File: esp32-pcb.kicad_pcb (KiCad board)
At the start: 2 copper layers, 25.2 x 59.4 mm, 50 parts, among them J1 Conn_01x15_Male, J2 Conn_01x15_Male, Q1 SI2333DDS-T1-GE3, Q2 BSS138Q-7-F, Q3 MMBT3904, Q4 MMBT3904, Q5 BSS138Q-7-F, SW1 RESET, SW2 USER, SW3 SW_DIP_x04, U1 XC6220B331MR, U2 ESP32-WROOM-32, U3 CP2102N-A01-GQFN24

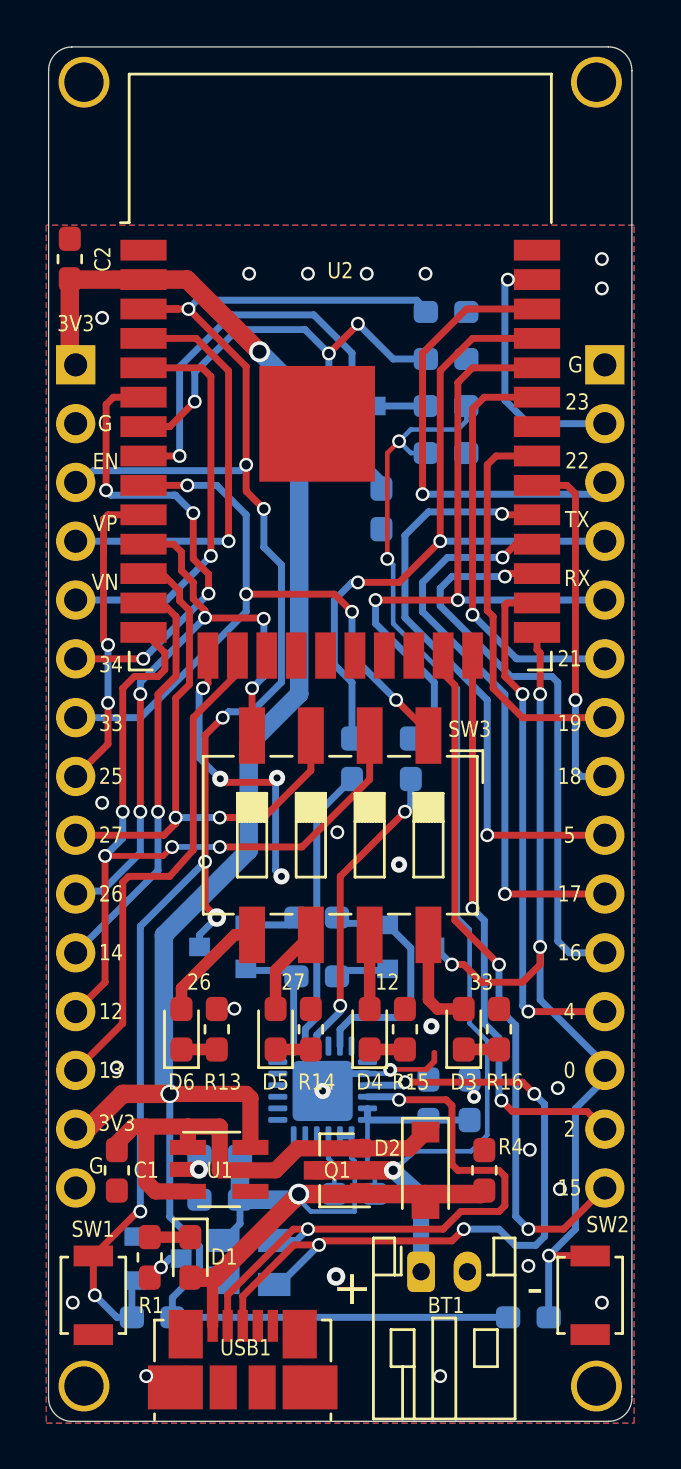
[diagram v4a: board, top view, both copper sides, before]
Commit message: Move C1 a bit, so that the left corner GND and 3V labels are more visible
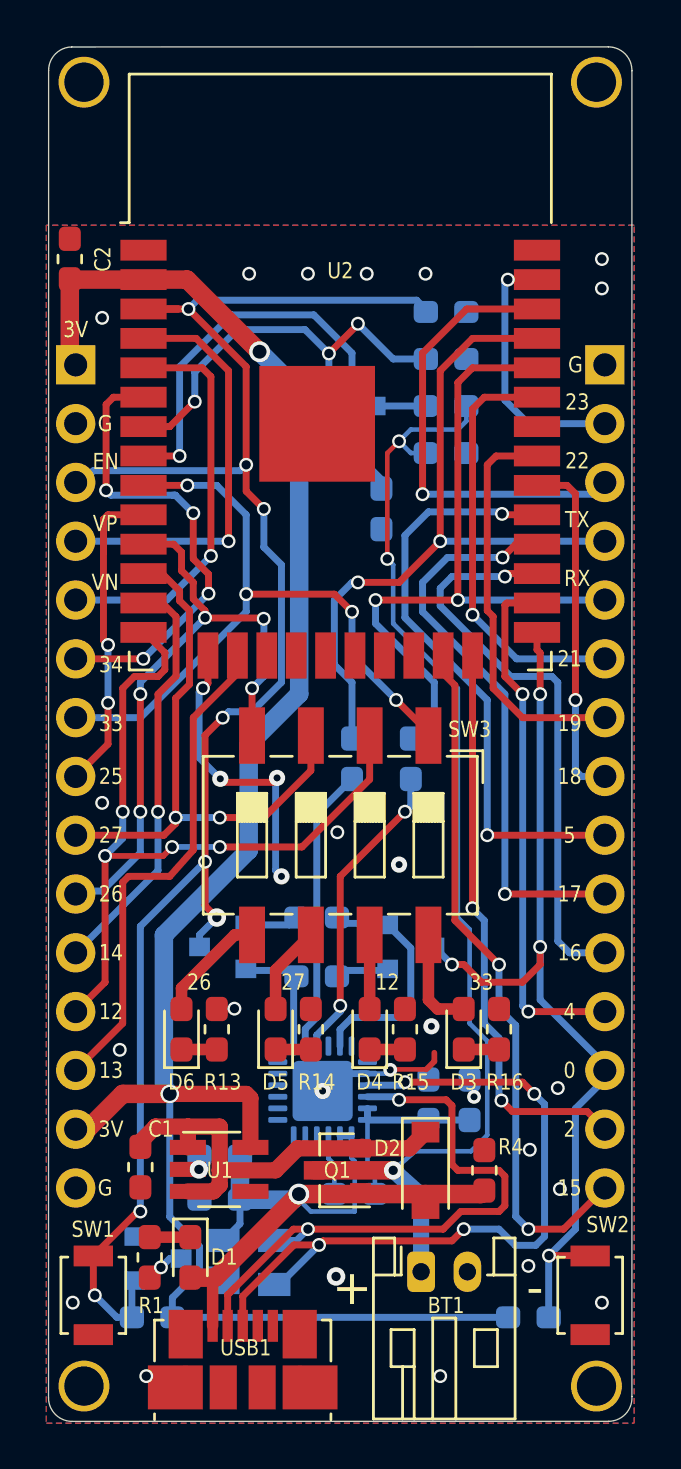
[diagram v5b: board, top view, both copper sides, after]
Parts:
- moved C1 1.03 mm to (133.1, 116.7)
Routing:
- net Net-(C1-Pad1): track 21.9 -> 18.5 mm
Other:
- board text added: "3V"
- board text removed: "3V3"
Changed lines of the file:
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@@
     (thickness 1.6)
     (drawings 3062)
-    (tracks 623)
+    (tracks 624)
     (zones 0)
     (modules 50)
@@
   )
   (setup
-    (last_trace_width 0.25)
+    (last_trace_width 0.7)
     (user_trace_width 0.2)
     (user_trace_width 0.25)
@@
   )
   (module Capacitor_SMD:C_0603_1608Metric_Pad1.05x0.95mm_HandSolder (layer F.Cu)
-    (at 132.08 116.84 270)
+    (at 133.096 116.699 270)
     (descr "Capacitor SMD 0603 (1608 Metric), square (rectangular) end terminal, IPC_7351 nominal with elongated pad for handsoldering. (Body size source: http://www.tortai-tech.com/upload/download/2011102023233369053.pdf), generated with kicad-footprint-generator")
     (tags "capacitor handsolder")
     (attr smd)
-    (fp_text reference C1 (at 0 -1.27) (layer F.SilkS)
+    (fp_text reference C1 (at -1.637 -0.889) (layer F.SilkS)
       (effects (font (size 0.7 0.6) (thickness 0.16)))
     )
@@
     (effects (font (size 0.7 0.6) (thickness 0.15)))
   )
-  (gr_text G (at 131.191 116.6495) (layer F.SilkS)
+  (gr_text G (at 131.572 117.602) (layer F.SilkS)
     (effects (font (size 0.7 0.6) (thickness 0.15)))
   )
-  (gr_text 3V3 (at 132.08 114.808) (layer F.SilkS)
+  (gr_text 3V (at 131.826 115.062) (layer F.SilkS)
     (effects (font (size 0.7 0.6) (thickness 0.15)))
   )
@@
     (effects (font (size 0.7 0.6) (thickness 0.15)))
   )
-  (gr_text 3V3 (at 130.302 80.264) (layer F.SilkS)
+  (gr_text 3V (at 130.302 80.518) (layer F.SilkS)
     (effects (font (size 0.7 0.6) (thickness 0.15)))
   )
@@
   (via (at 140.97 113.411) (size 0.7) (drill 0.3) (layers F.Cu B.Cu) (net 1) (status 30))
   (segment (start 142.9075 112.661) (end 141.72 112.661) (width 0.3) (layer B.Cu) (net 1) (status 30))
-  (via (at 145.669 110.617) (size 0.7) (drill 0.3) (layers F.Cu B.Cu) (net 1))
   (segment (start 136.549196 99.924804) (end 136.700392 100.076) (width 0.3) (layer F.Cu) (net 1))
   (via (at 136.549196 99.924804) (size 0.7) (drill 0.3) (layers F.Cu B.Cu) (net 1))
@@
   (segment (start 138.938 100.076) (end 138.938 103.886) (width 0.3) (layer B.Cu) (net 1))
   (segment (start 138.938 103.886) (end 139.192 104.14) (width 0.3) (layer B.Cu) (net 1))
-  (via (at 149.92 115.95) (size 0.6) (drill 0.4) (layers F.Cu B.Cu) (net 1))
-  (via (at 151.22 117.65) (size 0.6) (drill 0.4) (layers F.Cu B.Cu) (net 1))
-  (via (at 141.55 121.425) (size 0.8) (drill 0.4) (layers F.Cu B.Cu) (net 1))
-  (via (at 147.5105 113.665) (size 0.6) (drill 0.3) (layers F.Cu B.Cu) (net 1))
-  (via (at 149.86 120.9675) (size 0.6) (drill 0.4) (layers F.Cu B.Cu) (net 1))
-  (via (at 151.13 113.284) (size 0.6) (drill 0.4) (layers F.Cu B.Cu) (net 1))
-  (via (at 139.192 104.14) (size 0.7) (drill 0.3) (layers F.Cu B.Cu) (net 1))
-  (via (at 144.272 103.632) (size 0.7) (drill 0.3) (layers F.Cu B.Cu) (net 1))
-  (via (at 140.335 78.105) (size 0.6) (drill 0.4) (layers F.Cu B.Cu) (net 1))
-  (via (at 142.875 78.105) (size 0.6) (drill 0.4) (layers F.Cu B.Cu) (net 1))
-  (via (at 145.415 78.105) (size 0.6) (drill 0.4) (layers F.Cu B.Cu) (net 1))
-  (via (at 153.035 78.74) (size 0.6) (drill 0.4) (layers F.Cu B.Cu) (net 1))
-  (via (at 153.035 77.47) (size 0.6) (drill 0.4) (layers F.Cu B.Cu) (net 1))
-  (via (at 131.445 80.01) (size 0.6) (drill 0.4) (layers F.Cu B.Cu) (net 1))
-  (via (at 141.605 102.235) (size 0.6) (drill 0.4) (layers F.Cu B.Cu) (net 1))
-  (via (at 131.445 100.965) (size 0.6) (drill 0.4) (layers F.Cu B.Cu) (net 1))
-  (via (at 137.16 109.855) (size 0.6) (drill 0.4) (layers F.Cu B.Cu) (net 1))
-  (via (at 153.035 122.555) (size 0.6) (drill 0.4) (layers F.Cu B.Cu) (net 1))
-  (via (at 146.05 125.73) (size 0.6) (drill 0.4) (layers F.Cu B.Cu) (net 1))
-  (via (at 133.35 125.73) (size 0.6) (drill 0.4) (layers F.Cu B.Cu) (net 1))
-  (via (at 130.175 122.555) (size 0.6) (drill 0.4) (layers F.Cu B.Cu) (net 1))
+  (via (at 132.207 111.633) (size 0.6) (drill 0.4) (layers F.Cu B.Cu) (net 1))
   (via (at 137.795 78.105) (size 0.6) (drill 0.4) (layers F.Cu B.Cu) (net 1))
-  (via (at 132.08 112.395) (size 0.6) (drill 0.4) (layers F.Cu B.Cu) (net 1))
+  (via (at 130.175 122.555) (size 0.6) (drill 0.4) (layers F.Cu B.Cu) (net 1))
+  (via (at 133.35 125.73) (size 0.6) (drill 0.4) (layers F.Cu B.Cu) (net 1))
+  (via (at 146.05 125.73) (size 0.6) (drill 0.4) (layers F.Cu B.Cu) (net 1))
+  (via (at 153.035 122.555) (size 0.6) (drill 0.4) (layers F.Cu B.Cu) (net 1))
+  (via (at 137.16 109.855) (size 0.6) (drill 0.4) (layers F.Cu B.Cu) (net 1))
+  (via (at 131.445 100.965) (size 0.6) (drill 0.4) (layers F.Cu B.Cu) (net 1))
+  (via (at 141.605 102.235) (size 0.6) (drill 0.4) (layers F.Cu B.Cu) (net 1))
+  (via (at 131.445 80.01) (size 0.6) (drill 0.4) (layers F.Cu B.Cu) (net 1))
+  (via (at 153.035 77.47) (size 0.6) (drill 0.4) (layers F.Cu B.Cu) (net 1))
+  (via (at 153.035 78.74) (size 0.6) (drill 0.4) (layers F.Cu B.Cu) (net 1))
+  (via (at 145.415 78.105) (size 0.6) (drill 0.4) (layers F.Cu B.Cu) (net 1))
+  (via (at 142.875 78.105) (size 0.6) (drill 0.4) (layers F.Cu B.Cu) (net 1))
+  (via (at 140.335 78.105) (size 0.6) (drill 0.4) (layers F.Cu B.Cu) (net 1))
+  (via (at 144.272 103.632) (size 0.7) (drill 0.3) (layers F.Cu B.Cu) (net 1))
+  (via (at 139.192 104.14) (size 0.7) (drill 0.3) (layers F.Cu B.Cu) (net 1))
+  (via (at 151.13 113.284) (size 0.6) (drill 0.4) (layers F.Cu B.Cu) (net 1))
+  (via (at 149.86 120.9675) (size 0.6) (drill 0.4) (layers F.Cu B.Cu) (net 1))
+  (via (at 147.5105 113.665) (size 0.6) (drill 0.3) (layers F.Cu B.Cu) (net 1))
+  (via (at 141.55 121.425) (size 0.8) (drill 0.4) (layers F.Cu B.Cu) (net 1))
+  (via (at 151.22 117.65) (size 0.6) (drill 0.4) (layers F.Cu B.Cu) (net 1))
+  (via (at 149.92 115.95) (size 0.6) (drill 0.4) (layers F.Cu B.Cu) (net 1))
+  (via (at 145.669 110.617) (size 0.7) (drill 0.3) (layers F.Cu B.Cu) (net 1))
   (via (at 144.272 85.344) (size 0.6) (drill 0.4) (layers F.Cu B.Cu) (net 2))
   (via (at 143.764 90.424) (size 0.6) (drill 0.4) (layers F.Cu B.Cu) (net 2))
@@
   (segment (start 134.479 123.19) (end 134.479 122.3404) (width 0.3) (layer B.Cu) (net 3) (status 10))
   (segment (start 135.6487 121.1707) (end 135.6487 120.1293) (width 0.3) (layer B.Cu) (net 3))
-  (segment (start 137.85 115.85) (end 137.85 113.72) (width 0.7) (layer F.Cu) (net 3))
+  (segment (start 137.85 115.85) (end 137.85 113.72) (width 0.7) (layer F.Cu) (net 3) (status 10))
   (segment (start 137.668 113.538) (end 137.85 113.72) (width 0.7) (layer F.Cu) (net 3))
   (segment (start 134.366 113.538) (end 137.668 113.538) (width 0.7) (layer F.Cu) (net 3))
@@
   (segment (start 140.989883 119.888) (end 140.814952 120.062931) (width 0.3) (layer F.Cu) (net 69))
   (segment (start 146.558 119.888) (end 140.989883 119.888) (width 0.3) (layer F.Cu) (net 69))
-  (segment (start 132.08 115.67) (end 132.8 114.95) (width 0.7) (layer F.Cu) (net 72) (status 10))
   (segment (start 136.525 114.95) (end 136.525 116.84) (width 0.7) (layer F.Cu) (net 72))
-  (segment (start 133.35 117.348) (end 133.35 114.95) (width 0.7) (layer F.Cu) (net 72))
   (segment (start 142.68 115.815) (end 142.605 115.89) (width 0.7) (layer F.Cu) (net 72) (status 30))
   (segment (start 142.605 115.89) (end 139.888 115.89) (width 0.7) (layer F.Cu) (net 72) (status 10))
@@
   (segment (start 144.715 115.89) (end 145.415 115.19) (width 0.7) (layer F.Cu) (net 72) (status 20))
   (segment (start 142.605 115.89) (end 144.715 115.89) (width 0.7) (layer F.Cu) (net 72) (status 10))
-  (segment (start 135.15 115.85) (end 135.15 114.95) (width 0.7) (layer F.Cu) (net 72))
-  (segment (start 132.8 114.95) (end 135.15 114.95) (width 0.7) (layer F.Cu) (net 72))
+  (segment (start 135.15 115.85) (end 135.15 114.95) (width 0.7) (layer F.Cu) (net 72) (status 10))
   (segment (start 135.15 114.95) (end 136.525 114.95) (width 0.7) (layer F.Cu) (net 72))
-  (segment (start 133.752 117.75) (end 133.35 117.348) (width 0.7) (layer F.Cu) (net 72))
-  (segment (start 135.15 117.75) (end 133.752 117.75) (width 0.7) (layer F.Cu) (net 72))
-  (segment (start 132.08 115.965) (end 132.08 115.67) (width 0.5) (layer F.Cu) (net 72) (status 30))
+  (segment (start 133.752 114.956) (end 133.746 114.95) (width 0.7) (layer F.Cu) (net 72))
+  (segment (start 133.746 114.95) (end 135.15 114.95) (width 0.7) (layer F.Cu) (net 72))
+  (segment (start 133.096 115.612) (end 133.752 114.956) (width 0.7) (layer F.Cu) (net 72) (status 10))
+  (segment (start 133.096 115.824) (end 133.096 115.612) (width 0.7) (layer F.Cu) (net 72) (status 30))
+  (segment (start 135.15 117.75) (end 136.25 117.75) (width 0.7) (layer F.Cu) (net 72) (status 10))
+  (segment (start 136.525 117.475) (end 136.525 116.84) (width 0.7) (layer F.Cu) (net 72))
+  (segment (start 136.25 117.75) (end 136.525 117.475) (width 0.7) (layer F.Cu) (net 72))
   (segment (start 133.232 79.629) (end 134.747 79.629) (width 0.3) (layer F.Cu) (net 73) (status 10))
   (segment (start 137.668 82.122773) (end 135.174227 79.629) (width 0.3) (layer F.Cu) (net 73))
